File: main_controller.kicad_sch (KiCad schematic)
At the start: 38 parts, among them U1 STM32F303RETx, Y1 X322512MSB4SI

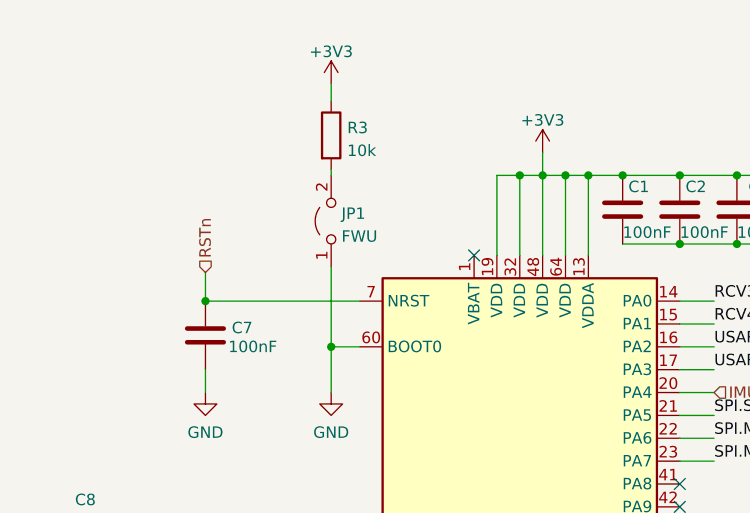
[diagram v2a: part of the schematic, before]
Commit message: Add finished PCB design for initial release
This is quite a messy version of the initial PCB, hopefully without
errors. Should conform to JLCPCB manufacturing process.
This is a 4 layer PCB with components on the TOP, test pads and
placement for debug connector on the bottom.
The inside layers consist of a ground plane and a layer for power
signals, especially 3v3 and BATT.
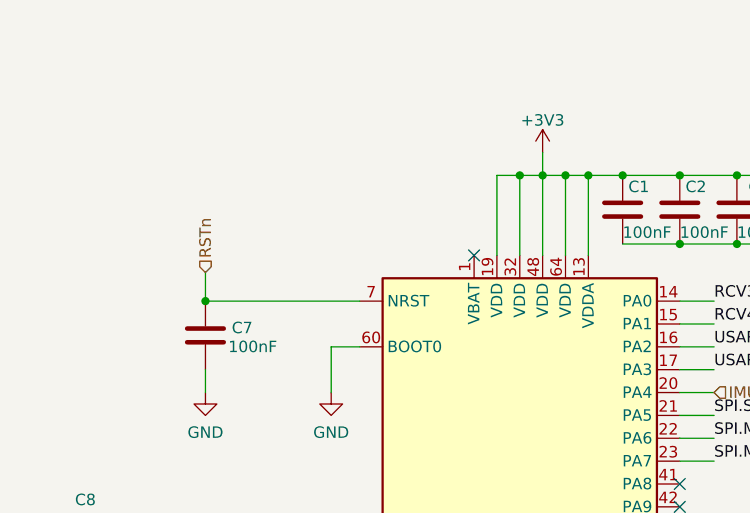
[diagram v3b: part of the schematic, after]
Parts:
- removed JP1: FWU, Connector_PinHeader_2.54mm:PinHeader_1x02_P2.54mm_Vertical, symbol Jumper:Jumper_2_Open
- removed R3: 10k, Resistor_SMD:R_0402_1005Metric, symbol Device:R
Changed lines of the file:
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@@
   (junction (at 54.61 83.82) (diameter 0) (color 0 0 0 0)
-  )
-  (junction (at 68.58 60.96) (diameter 0) (color 0 0 0 0)
   )
   (junction (at 100.965 41.91) (diameter 0) (color 0 0 0 0)
@@
     (stroke (width 0) (type default) (color 0 0 0 0))
   )
-  (wire (pts (xy 68.58 31.75) (xy 68.58 33.655))
-    (stroke (width 0) (type default) (color 0 0 0 0))
-  )
   (bus (pts (xy 183.515 114.935) (xy 183.515 117.475))
     (stroke (width 0) (type default) (color 0 0 0 0))
@@
     (stroke (width 0) (type default) (color 0 0 0 0))
   )
-  (wire (pts (xy 68.58 52.07) (xy 68.58 60.96))
-    (stroke (width 0) (type default) (color 0 0 0 0))
-  )
   (wire (pts (xy 67.945 83.82) (xy 67.945 86.36))
     (stroke (width 0) (type default) (color 0 0 0 0))
@@
   )
   (wire (pts (xy 68.58 60.96) (xy 71.755 60.96))
-    (stroke (width 0) (type default) (color 0 0 0 0))
-  )
-  (wire (pts (xy 68.58 41.275) (xy 68.58 41.91))
     (stroke (width 0) (type default) (color 0 0 0 0))
   )
@@
     (pin "1")
   )
-  (symbol (lib_id "power:+3V3") (at 68.58 31.75 0) (unit 1)
-    (in_bom yes) (on_board yes) (fields_autoplaced)
-    (property "Reference" "#PWR08" (id 0) (at 68.58 35.56 0)
-      (effects (font (size 1.27 1.27)) hide)
-    )
-    (property "Value" "+3V3" (id 1) (at 68.58 28.1742 0))
-    (property "Footprint" "" (id 2) (at 68.58 31.75 0)
-      (effects (font (size 1.27 1.27)) hide)
-    )
-    (property "Datasheet" "" (id 3) (at 68.58 31.75 0)
-      (effects (font (size 1.27 1.27)) hide)
-    )
-    (pin "1")
-  )
   (symbol (lib_id "power:+3V3") (at 217.805 61.595 0) (unit 1)
     (in_bom yes) (on_board yes) (fields_autoplaced)
@@
     )
     (pin "1")
-  )
-  (symbol (lib_id "Jumper:Jumper_2_Open") (at 68.58 46.99 90) (unit 1)
-    (in_bom yes) (on_board yes) (fields_autoplaced)
-    (property "Reference" "JP1" (id 0) (at 69.723 46.1553 90)
-      (effects (font (size 1.27 1.27)) (justify right))
-    )
-    (property "Value" "FWU" (id 1) (at 69.723 48.6922 90)
-      (effects (font (size 1.27 1.27)) (justify right))
-    )
-    (property "Footprint" "Connector_PinHeader_2.54mm:PinHeader_1x02_P2.54mm_Vertical" (id 2) (at 68.58 46.99 0)
-      (effects (font (size 1.27 1.27)) hide)
-    )
-    (property "Datasheet" "~" (id 3) (at 68.58 46.99 0)
-      (effects (font (size 1.27 1.27)) hide)
-    )
-    (pin "1")
-    (pin "2")
   )
   (symbol (lib_id "Connector:TestPoint") (at 130.81 167.64 0) (unit 1)
@@
     (pin "1")
   )
-  (symbol (lib_id "Device:R") (at 68.58 37.465 0) (unit 1)
-    (in_bom yes) (on_board yes) (fields_autoplaced)
-    (property "Reference" "R3" (id 0) (at 70.358 36.6303 0)
-      (effects (font (size 1.27 1.27)) (justify left))
-    )
-    (property "Value" "10k" (id 1) (at 70.358 39.1672 0)
-      (effects (font (size 1.27 1.27)) (justify left))
-    )
-    (property "Footprint" "Resistor_SMD:R_0402_1005Metric" (id 2) (at 66.802 37.465 90)
-      (effects (font (size 1.27 1.27)) hide)
-    )
-    (property "Datasheet" "~" (id 3) (at 68.58 37.465 0)
-      (effects (font (size 1.27 1.27)) hide)
-    )
-    (property "JLC" "0402" (id 4) (at 68.58 37.465 0)
-      (effects (font (size 1.27 1.27)) hide)
-    )
-    (property "LCSC" " C25744" (id 5) (at 68.58 37.465 0)
-      (effects (font (size 1.27 1.27)) hide)
-    )
-    (pin "1")
-    (pin "2")
-  )
   (symbol (lib_id "Device:C") (at 41.275 83.82 90) (unit 1)
